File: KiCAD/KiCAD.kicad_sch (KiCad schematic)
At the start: 0 parts

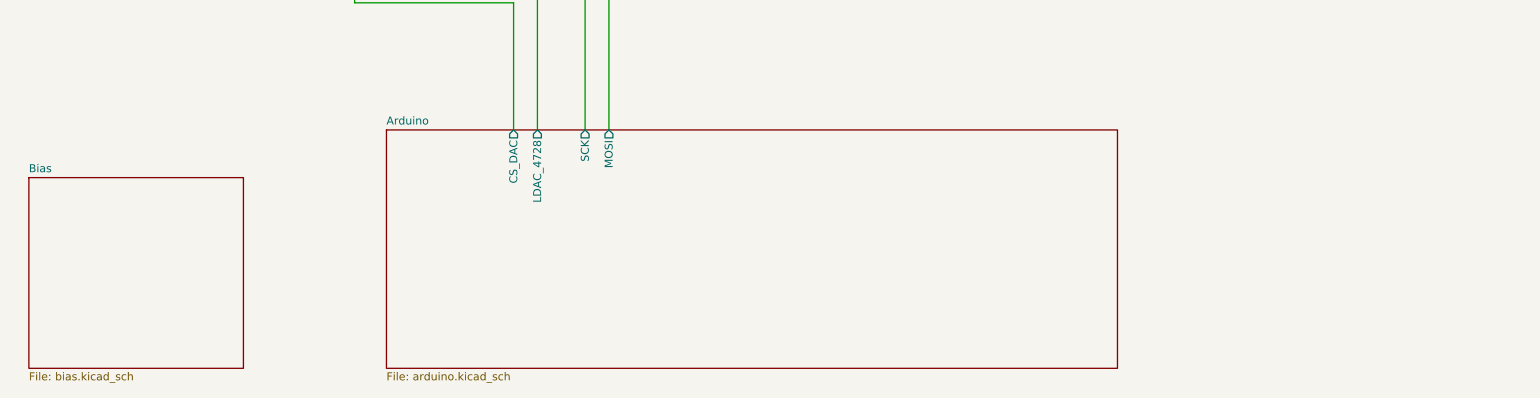
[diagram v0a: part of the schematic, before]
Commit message: interface: RJ45 umbilical sheet + RJE1D-188 footprint + open-items doc
Add KiCAD/interface.kicad_sch (page 10 of root) with SDA/SCL bidirectional
hierarchical labels, MBL_A/B differential outputs, and R100/R101 120-ohm
RS-422 terminators. Draft custom footprint Amphenol_RJE1D-188_Horizontal_Shielded
in xmitter.pretty -- signal pin array (P1-P8) is exact from datasheet;
shield-post, alignment-peg, and shield-tail hole coordinates are best-guess
and flagged for pre-fab verification.

Documentation/front_panel_interface.md is the single source of truth for
this subsystem: T568B pin map, single-point-ground rule, RS-422 termination
at the receiver end, plus an "Open items" checklist covering footprint
dimensions to verify, missing schematic pieces (RJ45 symbol, AM26LS32ACN
receiver, filament/HV/T-R relay drivers), and ruled-out parts (BSS138 level
shifter, MCP23017 expander, PCF8574 LCD backpack) so we don't re-propose
them.

build_checklist.md Phase 2 rewritten around the PCF8575-on-vector-board
approach; CLAUDE.md updated to reference the Interface sheet and the new
doc.

Co-Authored-By: Claude Opus 4.7 <noreply@anthropic.com>
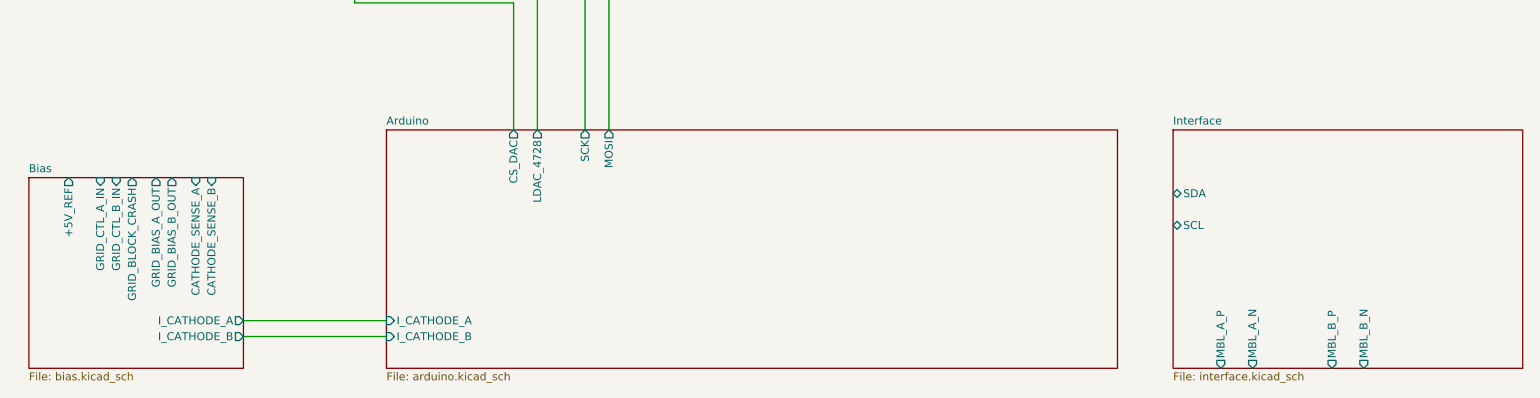
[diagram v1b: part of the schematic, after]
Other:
- added sheet Interface (interface.kicad_sch)
- sheet Arduino ports: added I_CATHODE_A, I_CATHODE_B; removed none
- sheet Bias ports: added +5V_REF, CATHODE_SENSE_A, CATHODE_SENSE_B, GRID_BIAS_A_OUT, GRID_BIAS_B_OUT, GRID_BLOCK_CRASH, GRID_CTL_A_IN, GRID_CTL_B_IN, I_CATHODE_A, I_CATHODE_B; removed none
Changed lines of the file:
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@@
+	(wire
+		(pts
+			(xy 67.31 139.7) (xy 90.17 139.7)
+		)
+		(stroke
+			(width 0)
+			(type default)
+		)
+	)
 	(wire
 		(pts
@@
 		(pts
 			(xy 99.06 73.66) (xy 99.06 59.69)
+		)
+		(stroke
+			(width 0)
+			(type default)
+		)
+	)
+	(wire
+		(pts
+			(xy 67.31 137.16) (xy 90.17 137.16)
 		)
 		(stroke
@@
 			)
 		)
+		(pin "I_CATHODE_A" input
+			(at 90.17 137.16 180)
+			(effects
+				(font
+					(size 1.27 1.27)
+				)
+				(justify left)
+			)
+		)
+		(pin "I_CATHODE_B" input
+			(at 90.17 139.7 180)
+			(effects
+				(font
+					(size 1.27 1.27)
+				)
+				(justify left)
+			)
+		)
 		(instances
 			(project "KiCAD"
@@
 	)
 	(sheet
+		(at 215.9 106.68)
+		(size 55.88 38.1)
+		(exclude_from_sim no)
+		(in_bom yes)
+		(on_board yes)
+		(dnp no)
+		(fields_autoplaced yes)
+		(stroke
+			(width 0.1524)
+			(type solid)
+		)
+		(fill
+			(color 0 0 0 0)
+		)
+		(property "Sheetname" "Interface"
+			(at 215.9 105.9684 0)
+			(show_name no)
+			(do_not_autoplace no)
+			(effects
+				(font
+					(size 1.27 1.27)
+				)
+				(justify left bottom)
+			)
+		)
+		(property "Sheetfile" "interface.kicad_sch"
+			(at 215.9 145.3646 0)
+			(show_name no)
+			(do_not_autoplace no)
+			(effects
+				(font
+					(size 1.27 1.27)
+				)
+				(justify left top)
+			)
+		)
+		(pin "SDA" bidirectional
+			(at 215.9 116.84 180)
+			(effects
+				(font
+					(size 1.27 1.27)
+				)
+				(justify left)
+			)
+		)
+		(pin "SCL" bidirectional
+			(at 215.9 121.92 180)
+			(effects
+				(font
+					(size 1.27 1.27)
+				)
+				(justify left)
+			)
+		)
+		(pin "MBL_A_P" output
+			(at 223.52 144.78 270)
+			(effects
+				(font
+					(size 1.27 1.27)
+				)
+				(justify right)
+			)
+		)
+		(pin "MBL_A_N" output
+			(at 228.6 144.78 270)
+			(effects
+				(font
+					(size 1.27 1.27)
+				)
+				(justify right)
+			)
+		)
+		(pin "MBL_B_P" output
+			(at 241.3 144.78 270)
+			(effects
+				(font
+					(size 1.27 1.27)
+				)
+				(justify right)
+			)
+		)
+		(pin "MBL_B_N" output
+			(at 246.38 144.78 270)
+			(effects
+				(font
+					(size 1.27 1.27)
+				)
+				(justify right)
+			)
+		)
+		(instances
+			(project "KiCAD"
+				(path "/d3de40b8-856b-4fbd-829c-f45ffcd55742"
+					(page "10")
+				)
+			)
+		)
+	)
+	(sheet
 		(at 33.02 114.3)
 		(size 34.29 30.48)
@@
 			)
 		)
+		(pin "+5V_REF" output
+			(at 39.37 114.3 90)
+			(effects
+				(font
+					(size 1.27 1.27)
+				)
+				(justify right)
+			)
+		)
+		(pin "CATHODE_SENSE_A" input
+			(at 59.69 114.3 90)
+			(effects
+				(font
+					(size 1.27 1.27)
+				)
+				(justify right)
+			)
+		)
+		(pin "CATHODE_SENSE_B" input
+			(at 62.23 114.3 90)
+			(effects
+				(font
+					(size 1.27 1.27)
+				)
+				(justify right)
+			)
+		)
+		(pin "GRID_BIAS_A_OUT" output
+			(at 53.34 114.3 90)
+			(effects
+				(font
+					(size 1.27 1.27)
+				)
+				(justify right)
+			)
+		)
+		(pin "GRID_BIAS_B_OUT" output
+			(at 55.88 114.3 90)
+			(effects
+				(font
+					(size 1.27 1.27)
+				)
+				(justify right)
+			)
+		)
+		(pin "GRID_BLOCK_CRASH" output
+			(at 49.53 114.3 90)
+			(effects
+				(font
+					(size 1.27 1.27)
+				)
+				(justify right)
+			)
+		)
+		(pin "GRID_CTL_A_IN" input
+			(at 44.45 114.3 90)
+			(effects
+				(font
+					(size 1.27 1.27)
+				)
+				(justify right)
+			)
+		)
+		(pin "GRID_CTL_B_IN" input
+			(at 46.99 114.3 90)
+			(effects
+				(font
+					(size 1.27 1.27)
+				)
+				(justify right)
+			)
+		)
+		(pin "I_CATHODE_A" output
+			(at 67.31 137.16 0)
+			(effects
+				(font
+					(size 1.27 1.27)
+				)
+				(justify right)
+			)
+		)
+		(pin "I_CATHODE_B" output
+			(at 67.31 139.7 0)
+			(effects
+				(font
+					(size 1.27 1.27)
+				)
+				(justify right)
+			)
+		)

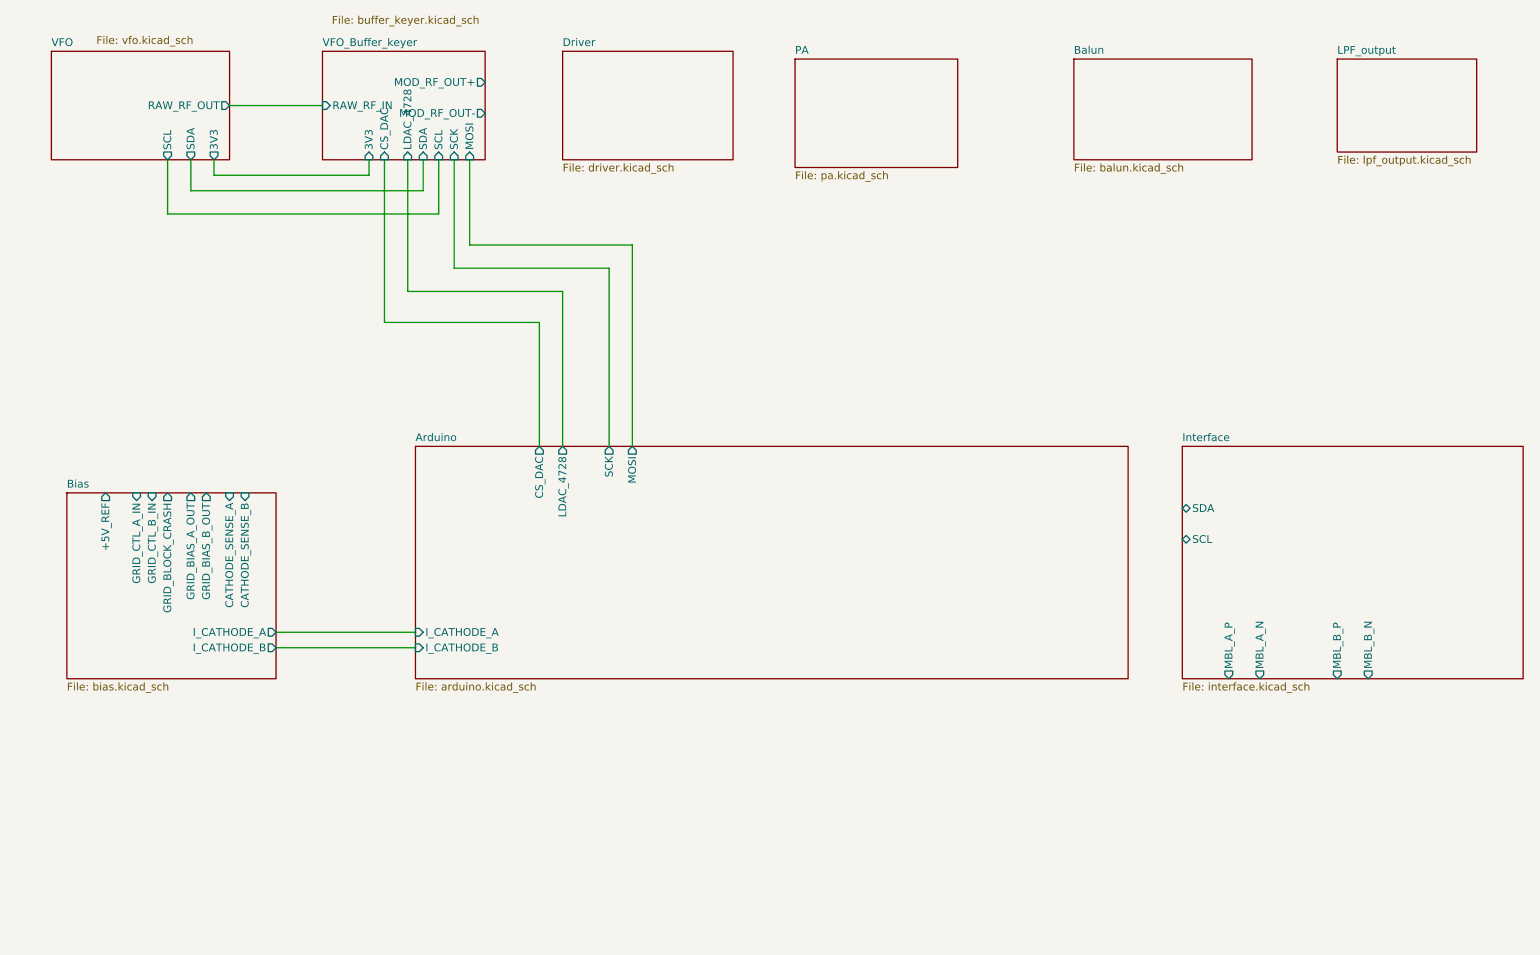
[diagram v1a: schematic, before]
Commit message: front-panel: QT encoder swap, PCF8575 breakout, pre-fab checklist, INT-none decision
Switch STEP + FUNC from direct PCF8575 GPIO to Adafruit I2C QT Rotary
Encoder breakouts (PID 4991) at addr 0x36 / 0x37. The onboard seesaw
SAMD09 handles quadrature decoding + button debounce, dropping ~200
lines of firmware. PCF8575 still covers the LCD (4-bit), paddle, and
panel LEDs.

Add custom KiCad symbols + footprints for both new breakouts to
xmitter.kicad_sym and xmitter.pretty. Footprint properties on the new
symbols are pre-linked, so schematic instances auto-associate. Some
coordinates in both footprints are best-guess pending physical
measurement -- flagged in the descr fields and in the new
front_panel_interface.md open-items subsections.

Decision documented (2026-07-03): no INT wiring back to the Metro.
Firmware polls all three I2C devices at 100 Hz; velocity-adaptive VFO
tuning is computed from delta-position / delta-time in the poll loop.
Rationale and a "here's how to add INT later" path in the new
"Interrupt handling (decision: none)" section of
front_panel_interface.md.

New Documentation/pcb_fab_checklist.md is the consolidated pre-flight
gate before analog-board gerbers ship -- nine sections covering
footprint verification, schematic completeness, ERC/DRC, physical, and
BOM sign-offs. build_checklist.md and CLAUDE.md updated to point at it.

Also in this bundle: SDA/SCL hierarchical labels changed to
bidirectional shape on the VFO, buffer_keyer, and interface sheets
(was an output/input polarity soup that would have failed ERC).
Interface and Front_Panel child sheets registered in .kicad_pro.
Front_Panel is an empty stub; components go in when the sheet is
populated. Adafruit PCF8575 and QT rotary encoder datasheets committed
under Documentation/Components/.

Co-Authored-By: Claude Opus 4.7 <noreply@anthropic.com>
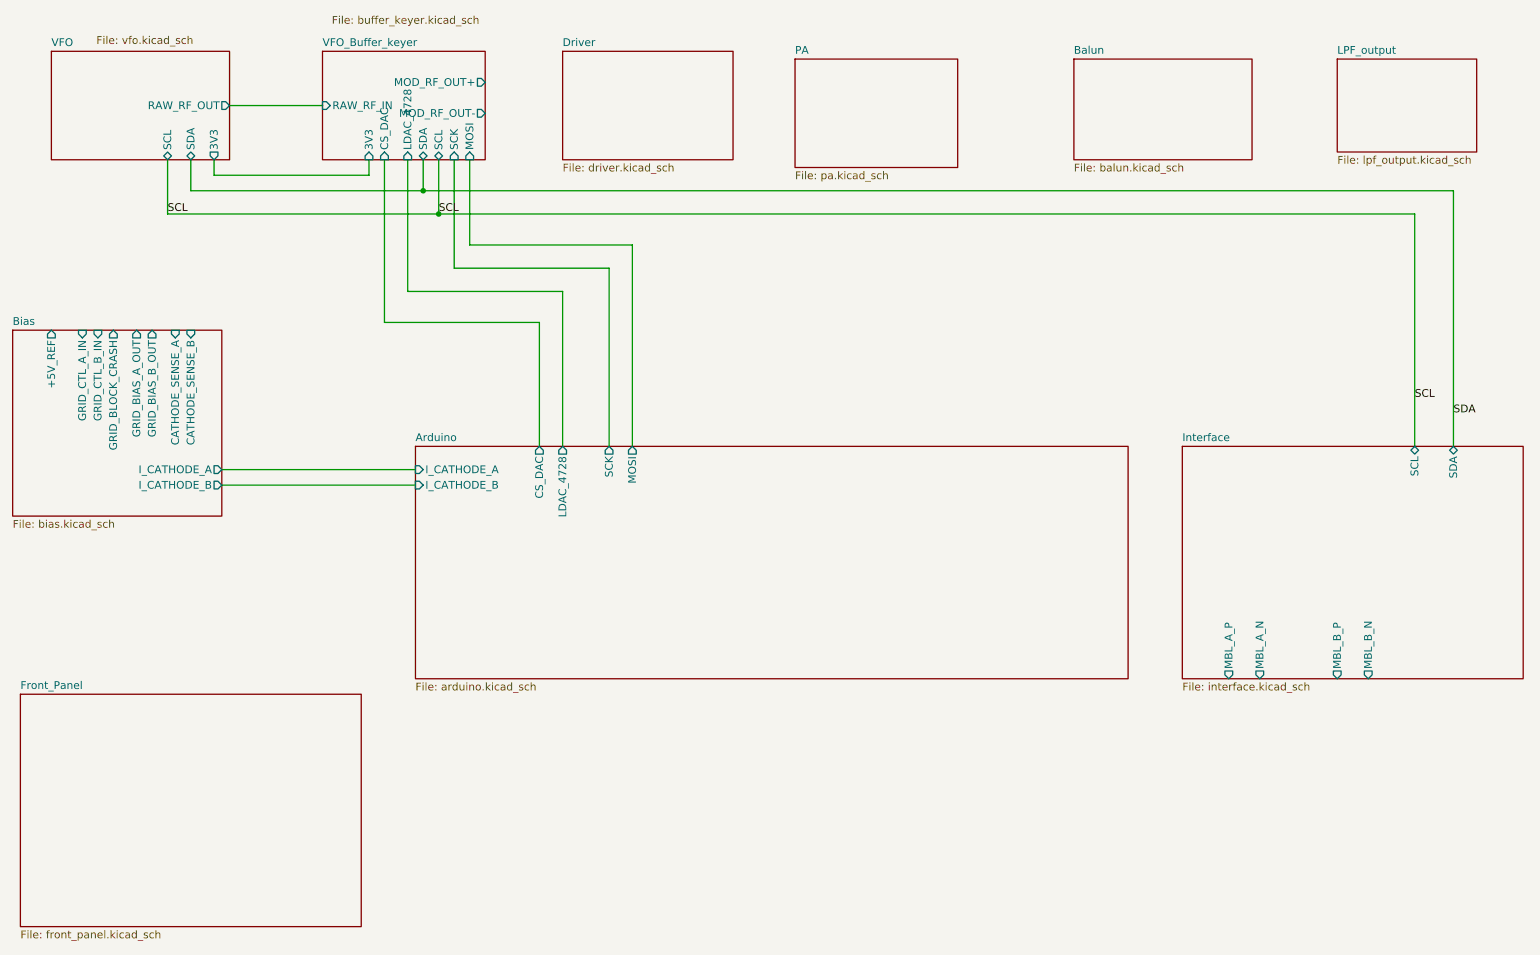
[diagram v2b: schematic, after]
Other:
- added sheet Front_Panel (front_panel.kicad_sch)
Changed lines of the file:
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@@
 	(generator_version "10.0")
 	(paper "A4")
+	(junction
+		(at 91.44 64.77)
+		(diameter 0)
+		(color 0 0 0 0)
+	)
+	(junction
+		(at 93.98 68.58)
+		(diameter 0)
+		(color 0 0 0 0)
+	)
 	(wire
 		(pts
@@
 	(wire
 		(pts
+			(xy 49.53 59.69) (xy 49.53 68.58)
+		)
+		(stroke
+			(width 0)
+			(type default)
+		)
+	)
+	(wire
+		(pts
+			(xy 260.35 64.77) (xy 260.35 106.68)
+		)
+		(stroke
+			(width 0)
+			(type default)
+		)
+	)
+	(wire
+		(pts
+			(xy 254 68.58) (xy 254 106.68)
+		)
+		(stroke
+			(width 0)
+			(type default)
+		)
+	)
+	(wire
+		(pts
 			(xy 57.15 62.23) (xy 82.55 62.23)
 		)
@@
 	(wire
 		(pts
+			(xy 121.92 77.47) (xy 96.52 77.47)
+		)
+		(stroke
+			(width 0)
+			(type default)
+		)
+	)
+	(wire
+		(pts
 			(xy 53.34 59.69) (xy 53.34 64.77)
 		)
@@
 	(wire
 		(pts
-			(xy 121.92 77.47) (xy 96.52 77.47)
-		)
-		(stroke
-			(width 0)
-			(type default)
-		)
-	)
-	(wire
-		(pts
-			(xy 91.44 64.77) (xy 91.44 59.69)
-		)
-		(stroke
-			(width 0)
-			(type default)
-		)
-	)
-	(wire
-		(pts
-			(xy 67.31 139.7) (xy 90.17 139.7)
+			(xy 58.42 113.03) (xy 90.17 113.03)
+		)
+		(stroke
+			(width 0)
+			(type default)
+		)
+	)
+	(wire
+		(pts
+			(xy 91.44 59.69) (xy 91.44 64.77)
 		)
 		(stroke
@@
 	(wire
 		(pts
+			(xy 254 68.58) (xy 93.98 68.58)
+		)
+		(stroke
+			(width 0)
+			(type default)
+		)
+	)
+	(wire
+		(pts
 			(xy 110.49 86.36) (xy 85.09 86.36)
 		)
@@
 	(wire
 		(pts
-			(xy 49.53 59.69) (xy 49.53 68.58)
-		)
-		(stroke
-			(width 0)
-			(type default)
-		)
-	)
-	(wire
-		(pts
 			(xy 125.73 106.68) (xy 125.73 73.66)
 		)
@@
 	(wire
 		(pts
+			(xy 91.44 64.77) (xy 260.35 64.77)
+		)
+		(stroke
+			(width 0)
+			(type default)
+		)
+	)
+	(wire
+		(pts
 			(xy 99.06 73.66) (xy 99.06 59.69)
 		)
@@
 	(wire
 		(pts
-			(xy 67.31 137.16) (xy 90.17 137.16)
+			(xy 58.42 110.49) (xy 90.17 110.49)
 		)
 		(stroke
@@
 			(width 0)
 			(type default)
+		)
+	)
+	(label "SCL"
+		(at 49.53 68.58 0)
+		(effects
+			(font
+				(size 1.27 1.27)
+			)
+			(justify left bottom)
+		)
+	)
+	(label "SCL"
+		(at 93.98 68.58 0)
+		(effects
+			(font
+				(size 1.27 1.27)
+			)
+			(justify left bottom)
+		)
+	)
+	(label "SDA"
+		(at 260.35 101.6 0)
+		(effects
+			(font
+				(size 1.27 1.27)
+			)
+			(justify left bottom)
+		)
+	)
+	(label "SCL"
+		(at 254 99.06 0)
+		(effects
+			(font
+				(size 1.27 1.27)
+			)
+			(justify left bottom)
 		)
 	)
@@
 		)
 		(pin "I_CATHODE_A" input
-			(at 90.17 137.16 180)
+			(at 90.17 110.49 180)
 			(effects
 				(font
@@
 		)
 		(pin "I_CATHODE_B" input
-			(at 90.17 139.7 180)
+			(at 90.17 113.03 180)
 			(effects
 				(font
@@
 		)
 		(pin "SDA" bidirectional
-			(at 215.9 116.84 180)
-			(effects
-				(font
-					(size 1.27 1.27)
-				)
-				(justify left)
+			(at 260.35 106.68 90)
+			(effects
+				(font
+					(size 1.27 1.27)
+				)
+				(justify right)
 			)
 		)
 		(pin "SCL" bidirectional
-			(at 215.9 121.92 180)
-			(effects
-				(font
-					(size 1.27 1.27)
-				)
-				(justify left)
+			(at 254 106.68 90)
+			(effects
+				(font
+					(size 1.27 1.27)
+				)
+				(justify right)
 			)
 		)
@@
 					(size 1.27 1.27)
 				)
-				(justify right)
+				(justify left)
 			)
 		)
@@
 					(size 1.27 1.27)
 				)
-				(justify right)
+				(justify left)
 			)
 		)
@@
 					(size 1.27 1.27)
 				)
-				(justify right)
+				(justify left)
 			)
 		)
@@
 					(size 1.27 1.27)
 				)
-				(justify right)
+				(justify left)
 			)
 		)
@@
 	)
 	(sheet
-		(at 33.02 114.3)
+		(at 25.4 147.32)
+		(size 55.88 38.1)
+		(exclude_from_sim no)
+		(in_bom yes)
+		(on_board yes)
+		(dnp no)
+		(fields_autoplaced yes)
+		(stroke
+			(width 0.1524)
+			(type solid)
+		)
+		(fill
+			(color 0 0 0 0)
+		)
+		(property "Sheetname" "Front_Panel"
+			(at 25.4 146.6084 0)
+			(show_name no)
+			(do_not_autoplace no)
+			(effects
+				(font
+					(size 1.27 1.27)
+				)
+				(justify left bottom)
+			)
+		)
+		(property "Sheetfile" "front_panel.kicad_sch"
+			(at 25.4 186.0046 0)
+			(show_name no)
+			(do_not_autoplace no)
+			(effects
+				(font
+					(size 1.27 1.27)
+				)
+				(justify left top)
+			)
+		)
+		(instances
+			(project "KiCAD"
+				(path "/d3de40b8-856b-4fbd-829c-f45ffcd55742"
+					(page "11")
+				)
+			)
+		)
+	)
+	(sheet
+		(at 24.13 87.63)
 		(size 34.29 30.48)
 		(exclude_from_sim no)
@@
 		)
 		(property "Sheetname" "Bias"
-			(at 33.02 113.5884 0)
+			(at 24.13 86.9184 0)
 			(show_name no)
 			(do_not_autoplace no)
@@
 		)
 		(property "Sheetfile" "bias.kicad_sch"
-			(at 33.02 145.3646 0)
+			(at 24.13 118.6946 0)
 			(show_name no)
 			(do_not_autoplace no)
@@
 		)
 		(pin "+5V_REF" output
-			(at 39.37 114.3 90)
+			(at 30.48 87.63 90)
 			(effects
 				(font
@@
 		)
 		(pin "CATHODE_SENSE_A" input
-			(at 59.69 114.3 90)
+			(at 50.8 87.63 90)
 			(effects
 				(font
@@
 		)
 		(pin "CATHODE_SENSE_B" input
-			(at 62.23 114.3 90)
+			(at 53.34 87.63 90)
 			(effects
 				(font
@@
 		)
 		(pin "GRID_BIAS_A_OUT" output
-			(at 53.34 114.3 90)
+			(at 44.45 87.63 90)
 			(effects
 				(font
@@
 		)
 		(pin "GRID_BIAS_B_OUT" output
-			(at 55.88 114.3 90)
+			(at 46.99 87.63 90)
 			(effects
 				(font
@@
 		)
 		(pin "GRID_BLOCK_CRASH" output
-			(at 49.53 114.3 90)
+			(at 40.64 87.63 90)
 			(effects
 				(font
@@
 		)
 		(pin "GRID_CTL_A_IN" input
-			(at 44.45 114.3 90)
+			(at 35.56 87.63 90)
 			(effects
 				(font
@@
 		)
 		(pin "GRID_CTL_B_IN" input
-			(at 46.99 114.3 90)
+			(at 38.1 87.63 90)
 			(effects
 				(font
@@
 		)
 		(pin "I_CATHODE_A" output
-			(at 67.31 137.16 0)
+			(at 58.42 110.49 0)
 			(effects
 				(font
@@
 		)
 		(pin "I_CATHODE_B" output
-			(at 67.31 139.7 0)
+			(at 58.42 113.03 0)
 			(effects
 				(font
@@
 			)
 		)
-		(pin "SCL" input
+		(pin "SCL" bidirectional
 			(at 93.98 59.69 270)
 			(effects
@@
 			)
 		)
-		(pin "SDA" input
+		(pin "SDA" bidirectional
 			(at 91.44 59.69 270)
 			(effects
@@
 			)
 		)
-		(pin "SCL" output
+		(pin "SCL" bidirectional
 			(at 49.53 59.69 270)
 			(effects
@@
 			)
 		)
-		(pin "SDA" output
+		(pin "SDA" bidirectional
 			(at 53.34 59.69 270)
 			(effects
